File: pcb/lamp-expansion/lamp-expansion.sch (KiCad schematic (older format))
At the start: 18 parts

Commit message: schematic work for expansion board
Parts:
- added BT?: LIPO, symbol LIPO
- added C? (x2): 22uF, symbol C_POL
- added C? (x2): 10uF, symbol C_POL
- added D?: PMEG2020CPA, symbol SCHOTTKY_DUAL-CC
- added D?: MSS2P2, symbol D_SCHOTTKY
- added IC?: LM1117_5.0, symbol LM1117
- added J?: 6-15V, symbol DCIN
- C?: value 4.7uF -> 10uF; Distrib. Part (none) -> 587-1353-1-ND; Distributor (none) -> Digikey; Manuf. Part (none) -> Taiyo Yuden; Manufacturer (none) -> TMK316F106ZL-T
- IC?: value LM1117 -> LM1117_3.3; Distrib. Part (none) -> AP1117IE33G-13DICT-ND; Distributor (none) -> Digikey; Manuf. Part (none) -> AP1117IE33G-13; Manufacturer (none) -> Diodes Incorporated
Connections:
- net labels added: +5V, +BATT, DC_IN, VCC, V_DC
- wire segments 45 -> 71
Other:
- note added: "DC input and 3.3V LDO"
- note added: "lithium polymer battery and charger"
- moved on the sheet: IC?

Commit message: work in progress
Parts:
- removed D?: PMEG2020CPA, symbol SCHOTTKY_DUAL-CC
- added C? (x4): 1uF, symbol C
- added C? (x2): 0.1uF, symbol C
- added D? (x2): MSS2P2, symbol D_SCHOTTKY
- added IC?: MCP73811, symbol MCP73811/2
- added IC?: AP2411, symbol AP24x1
- added IC?: TLV1117LV28, symbol LM1117
- added JP?: WIFI-LOG-LVL, symbol JUMPER
- added JP?: BAT-TO-REG, symbol JUMPER
- added JP?: BAT-TO-VCC, symbol JUMPER-CLOSED
- added J_SPI: 2x3PIN_FEMALE, symbol 6PIN_FEMALE
- added J_UART: 6PIN_FEMALE, symbol 6PIN_FEMALE
- added R?: 10kΩ, symbol R
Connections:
- net labels added: AVR_MISO, AVR_MOSI, AVR_RST, AVR_SCK, V_BAT, V_IO
- net labels removed: DC_IN
- wire segments 71 -> 156
- no-connect marks 2 -> 3
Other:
- note added: "2.8V regulator for wifi logic level"
- note added: "3.3V jumper for wifi logic level"
- note added: "5V charger input"
- note added: "battery and charger"
- note added: "battery voltage switching jumpers"
- note added: "lithium polymer battery, charger, and power switch"
- note added: "power switch"
- note removed: "lithium polymer battery and charger"
- moved on the sheet: BT?, C?, D?, F?, IC?, J?, R?, RX, TX

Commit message: cc3000 schematic diagram done
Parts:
- removed JP?: WIFI-LOG-LVL, symbol JUMPER
- removed JP?: BAT-TO-REG, symbol JUMPER
- removed JP?: BAT-TO-VCC, symbol JUMPER-CLOSED
- added AE?: ANTENNA, symbol ANTENNA
- added C? (x2): 1uF, symbol C
- added C?: 10pF, symbol C
- added C?: 2.2pF, symbol C
- added C?: DNP(10pF), symbol C
- added J?: UF.L, symbol COAX-JACK
- added JP?: VBAT-DIR-SELECT, symbol JUMPER_3-PIN-CLOSED
- added JP?: WIFI-LOG-LVL-SEL, symbol JUMPER_2-PIN
- added JP?: MODE-SEL, symbol JUMPER_3-PIN-CLOSED
- added L?: 2.2nH, symbol L
- added L?: DNP, symbol L
- added R?: 0Ω, symbol R
- added TP1, TP2, TP3, TP4, TP5: TEST, symbol TEST
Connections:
- net labels added: CC_EN, CC_IRQ, CC_MISO, CC_MOSI, CC_SCK, CC_SEL
- wire segments 156 -> 187
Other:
- note added: "CC3000 wifi module"
- note added: "optional external antenna jack"
- note added: "wifi logic 3.3V jumper"
- note removed: "3.3V jumper for wifi logic level"
- moved on the sheet: BT?, C?, D?, F?, IC?, J?, J_SPI, J_UART, R?, RX, TX

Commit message: moving to work on main board
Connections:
- net GND: now also C?.1
- net VCC: now also C?.2, IC?.19 (VBAT_IN)
- net V_FTDI: now also IC?.10 (3V3OUT)
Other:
- moved on the sheet: D?, J?
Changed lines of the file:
@@
 L DCIN J?
 U 1 1 5355B2AC
-P 1500 6350
-F 0 "J?" H 1450 6100 60  0000 C CNN
-F 1 "6-15V" H 1500 6000 60  0000 C CNN
-F 2 "" H 1500 6350 60  0000 C CNN
-F 3 "" H 1500 6350 60  0000 C CNN
-	1    1500 6350
+P 1600 6350
+F 0 "J?" H 1550 6100 60  0000 C CNN
+F 1 "6-15V" H 1600 6000 60  0000 C CNN
+F 2 "" H 1600 6350 60  0000 C CNN
+F 3 "" H 1600 6350 60  0000 C CNN
+	1    1600 6350
 	1    0    0    -1
 $EndComp
@@
 L GND #PWR?
 U 1 1 5355B2CA
-P 1850 6500
-F 0 "#PWR?" H 1850 6500 30  0001 C CNN
-F 1 "GND" H 1850 6430 30  0001 C CNN
-F 2 "" H 1850 6500 60  0000 C CNN
-F 3 "" H 1850 6500 60  0000 C CNN
-	1    1850 6500
+P 1950 6500
+F 0 "#PWR?" H 1950 6500 30  0001 C CNN
+F 1 "GND" H 1950 6430 30  0001 C CNN
+F 2 "" H 1950 6500 60  0000 C CNN
+F 3 "" H 1950 6500 60  0000 C CNN
+	1    1950 6500
 	1    0    0    -1
 $EndComp
@@
 	0    1    1    0
 $EndComp
-Text Label 2550 6300 2    60   ~ 0
+Text Label 2650 6300 2    60   ~ 0
 V_DC
 $Comp
@@
 	3700 8400 3700 8200
 Wire Wire Line
-	3700 8200 4200 8200
+	3700 8200 4300 8200
 Wire Wire Line
 	5400 8700 5300 8700
@@
 	5850 8300 5300 8300
 Wire Wire Line
-	1850 6500 1850 6400
-Wire Wire Line
-	1850 6400 1750 6400
+	1950 6500 1950 6400
+Wire Wire Line
+	1950 6400 1850 6400
 Wire Wire Line
 	3350 6200 3750 6200
@@
 L D_SCHOTTKY D?
 U 1 1 5356B181
-P 2000 6300
-F 0 "D?" H 2000 6500 60  0000 C CNN
-F 1 "MSS2P2" H 2000 6400 60  0000 C CNN
-F 2 "" H 1750 6300 60  0001 C CNN
-F 3 "" H 1850 6400 60  0001 C CNN
-F 4 "Vishay" H 2000 6300 60  0001 C CNN "Manufacturer"
-F 5 "MSS2P2-M3/89A" H 2000 6300 60  0001 C CNN "Manuf. Part"
-F 6 "Digikey" H 2000 6300 60  0001 C CNN "Distributor"
-F 7 "MSS2P2-M3/89AGICT-ND" H 2000 6300 60  0001 C CNN "Distrib. Part"
-	1    2000 6300
-	1    0    0    -1
-$EndComp
-Wire Wire Line
-	1750 6300 1850 6300
-Wire Wire Line
-	2550 6300 2150 6300
+P 2100 6300
+F 0 "D?" H 2100 6500 60  0000 C CNN
+F 1 "MSS2P2" H 2100 6400 60  0000 C CNN
+F 2 "" H 1850 6300 60  0001 C CNN
+F 3 "" H 1950 6400 60  0001 C CNN
+F 4 "Vishay" H 2100 6300 60  0001 C CNN "Manufacturer"
+F 5 "MSS2P2-M3/89A" H 2100 6300 60  0001 C CNN "Manuf. Part"
+F 6 "Digikey" H 2100 6300 60  0001 C CNN "Distributor"
+F 7 "MSS2P2-M3/89AGICT-ND" H 2100 6300 60  0001 C CNN "Distrib. Part"
+	1    2100 6300
+	1    0    0    -1
+$EndComp
+Wire Wire Line
+	1850 6300 1950 6300
+Wire Wire Line
+	2650 6300 2250 6300
 Wire Wire Line
 	3200 6600 3500 6600
@@
 	0    -1   -1   0
 $EndComp
-Wire Wire Line
-	14250 5150 14050 5150
 $Comp
 L GND #PWR?
@@
 U 1 1 53570C4B
 P 14150 4650
-F 0 "C?" V 14150 4950 60  0000 C CNN
+F 0 "C?" V 14150 5000 60  0000 C CNN
 F 1 "1uF" V 14250 5000 60  0000 C CNN
 F 2 "" H 14150 4650 60  0001 C CNN
@@
 F 3 "" H 14250 5350 60  0000 C CNN
 	1    14250 5350
-	0    1    1    0
-$EndComp
-$Comp
-L C C?
-U 1 1 5357209E
-P 14150 5250
-F 0 "C?" V 14100 5600 60  0000 C CNN
-F 1 "1uF" V 14200 5600 60  0000 C CNN
-F 2 "" H 14150 5250 60  0001 C CNN
-F 3 "" H 14150 5250 60  0001 C CNN
-	1    14150 5250
 	0    1    1    0
 $EndComp
@@
 Wire Notes Line
 	14650 6600 13500 6600
+Wire Wire Line
+	14050 5350 14250 5350
+Connection ~ 14150 5350
+$Comp
+L C C?
+U 1 1 5357209E
+P 14150 5250
+F 0 "C?" V 14100 5600 60  0000 C CNN
+F 1 "1uF" V 14200 5600 60  0000 C CNN
+F 2 "" H 14150 5250 60  0001 C CNN
+F 3 "" H 14150 5250 60  0001 C CNN
+	1    14150 5250
+	0    1    1    0
+$EndComp
+Wire Wire Line
+	14050 5150 14250 5150
+Connection ~ 14150 5150
 $EndSCHEMATC

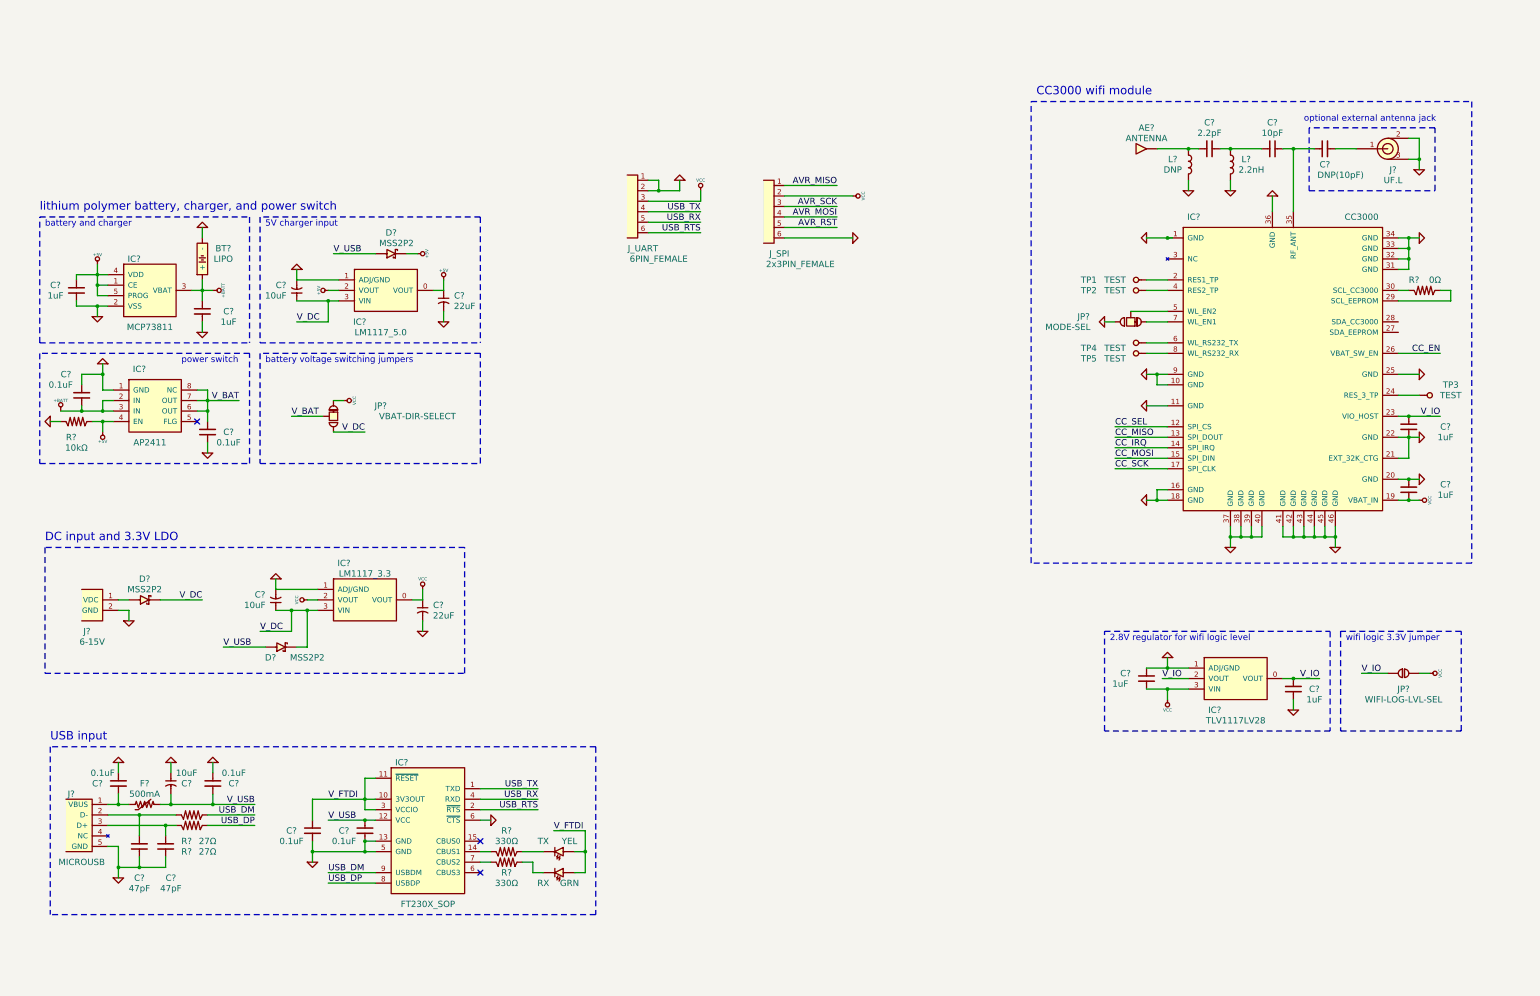
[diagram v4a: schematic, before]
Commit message: still need to add boost reg to schematic;
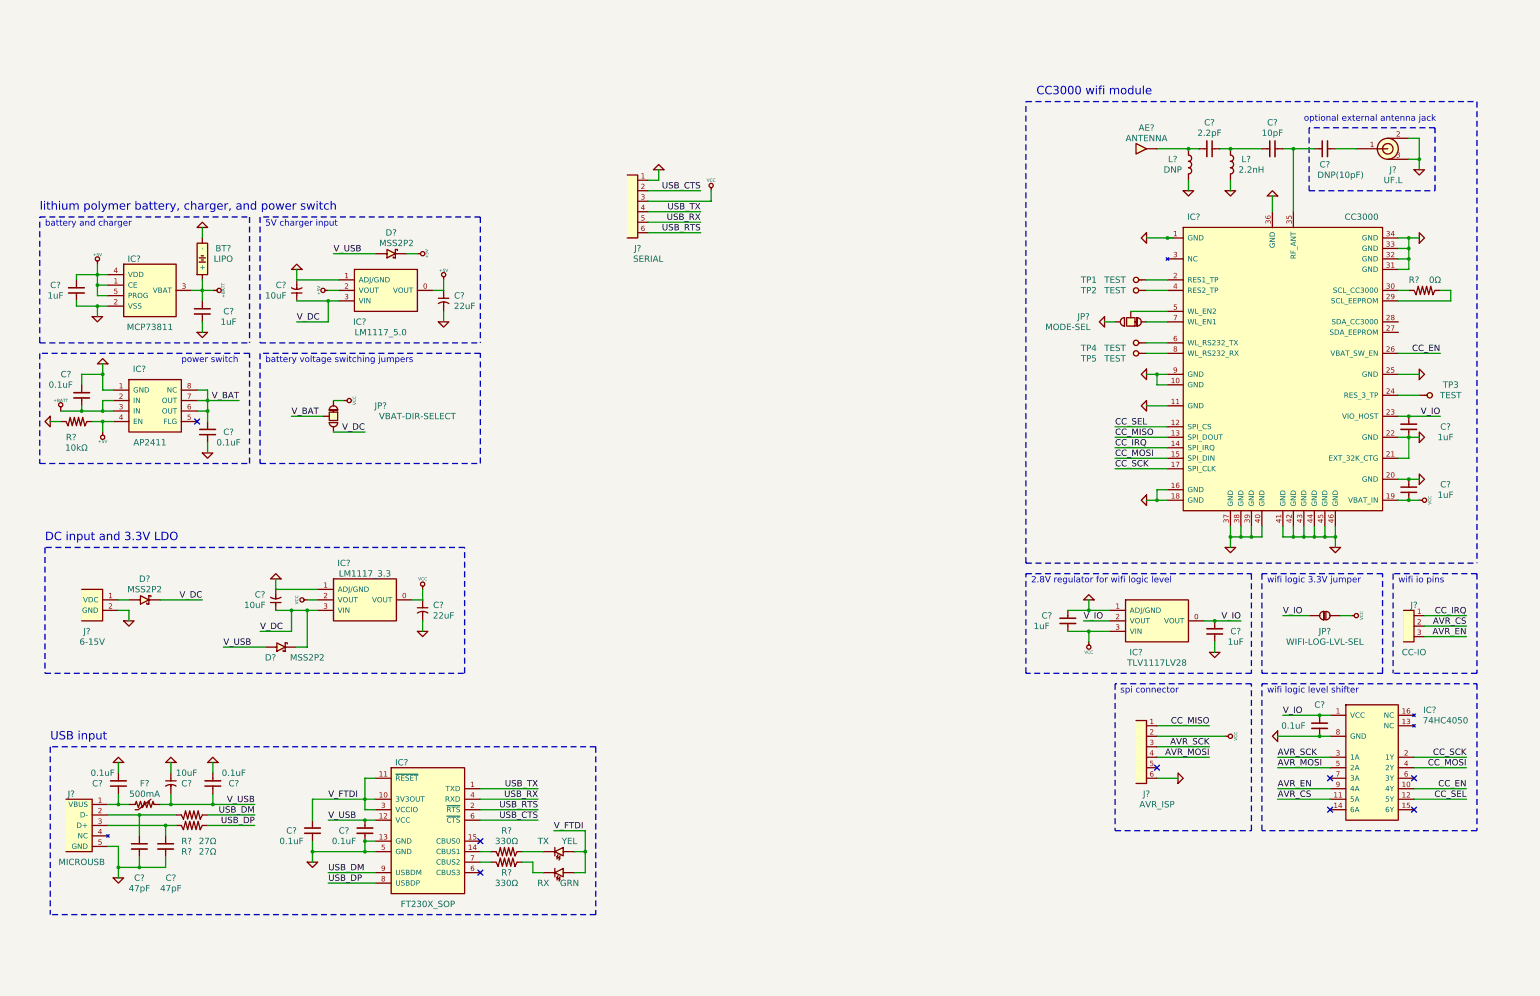
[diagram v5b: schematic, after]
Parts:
- added C?: 0.1uF, symbol C
- added IC?: 74HC4050, symbol 74HC4050
- added J?: CC-IO, symbol 3PIN_FEMALE
- J?: renamed from J_UART; value 6PIN_FEMALE -> SERIAL
- J?: renamed from J_SPI; value 2x3PIN_FEMALE -> AVR_ISP
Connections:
- net AVR_MISO is gone; now on net CC_MISO: J?.1
- net AVR_MOSI: now also IC?.5 (2A)
- net AVR_SCK: now also IC?.3 (1A)
- net CC_EN: now also IC?.10 (4Y)
- net CC_IRQ: now also J?.1
- net CC_MOSI: now also IC?.4 (2Y)
- net CC_SCK: now also IC?.2 (1Y)
- net CC_SEL: now also IC?.12 (5Y)
- net GND: now also C?.2, IC?.8 (GND); no longer IC?.6 (~CTS~), J?.2
- net V_IO: now also C?.1, IC?.1 (VCC)
- net USB_CTS: now reaches IC?.6 (~CTS~)
- net USB_CTS: now also J?.2
- net AVR_RST: no longer names the net of J?.5
- new net AVR_CS: IC?.11 (5A), J?.2
- new net AVR_EN: IC?.9 (4A), J?.3
- no-connect marks 3 -> 8
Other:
- note added: "spi connector"
- note added: "wifi io pins"
- note added: "wifi logic level shifter"
- moved on the sheet: C?, IC?, J?, JP?

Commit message: expansion schematic nearly done
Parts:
- removed C? (x2): 22uF, symbol C_POL
- added C?: 4.7pF, symbol C_POL
- added C? (x3): 22uF, symbol C_POL
- added C? (x2): 0.1uF, symbol C
- added C?: 100uF, symbol C_POL
- added D? (x2): 3A, symbol D_SCHOTTKY
- added IC?: LM2623_VSSOP, symbol LM2623_VSSOP
- added IC?: 78L50_SOT, symbol 78LXX_SOT
- added JP?: I-TEST, symbol JUMPER_2-PIN-CLOSED
- added L?: 4.7uH, symbol L
- added Q?: 2N7002, symbol N-CHAN-MOSFET_SOT
- added R?: 10k, symbol R
- added R?: 150kΩ, symbol R
- added R?: 430kΩ, symbol R
- added R?: 91kΩ, symbol R
- J?: value 6-15V -> 7-15V
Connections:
- net +5V: now also C?.1
- net GND: now also C?.1, C?.2, C?.2, C?.2, C?.2, C?.2, IC?.1 (PGND), IC?.5 (SGND), Q?.2 (S), R?.2
- net VCC: now also C?.1
- net V_BAT: now also C?.1, D?.1 (C), D?.2 (A), L?.1, R?.2
- net V_USB: now also D?.2 (A)
- net DC_IN: now reaches D?.2 (A), J?.1 (VDC)
- net DC_IN: now also Q?.1 (G)
- new net: IC?.2 (EN), Q?.3 (D), R?.1
- new net: C?.1, IC?.3 (FREQ), R?.1
- new net: IC?.4 (FB), R?.1, R?.2
- new net: C?.2, IC?.6 (VDD), R?.2
- new net: C?.2, IC?.8 (SW), JP?.1
- new net: JP?.1, L?.2
- new net V_LED: C?.1, C?.1, D?.1 (C), IC?.7 (BOOT), R?.1
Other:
- note added: "USB / battery to 7V boost regulator"
- moved on the sheet: AE?, BT?, C?, D?, F?, IC?, J?, JP?, L?, R?, RX, TP1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

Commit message: i think the schematic is done
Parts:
- added J? (x2): 2PIN_POWER, symbol 2PIN_FEMALE
- added J?: 2PIN_IO, symbol 2PIN_FEMALE
- added J?: 5PIN_INPUT, symbol 5PIN_FEMALE
- added R? (x2): 10kΩ, symbol R
- added S? (x2): SPST, symbol SPST
- added TP? (x7): PIN, symbol TEST
- added VR? (x3): 100kΩ, symbol POT
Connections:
- net GND: now also J?.2, J?.2, S?.1, S?.1, VR?.3 (E2), VR?.3 (E2), VR?.3 (E2)
- net VCC: now also J?.1, R?.1, R?.1, VR?.1 (E1), VR?.1 (E1), VR?.1 (E1)
- net V_LED: now also J?.1
- new net AVR_0: J?.1, TP?.1 (TP)
- new net AVR_1: J?.2, TP?.1 (TP)
- new net POT_0: J?.1, TP?.1 (TP), VR?.2 (W)
- new net POT_1: J?.2, TP?.1 (TP), VR?.2 (W)
- new net POT_2: J?.3, TP?.1 (TP), VR?.2 (W)
- new net SW_0: J?.4, R?.2, S?.2, TP?.1 (TP)
- new net SW_1: J?.5, R?.2, S?.2, TP?.1 (TP)
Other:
- note added: "buttons"
- note added: "buttons and pots header"
- note added: "extra io"
- note added: "potentiometers"
- note added: "power headers"
- note added: "serial header"
- note added: "user input"
- moved on the sheet: J?

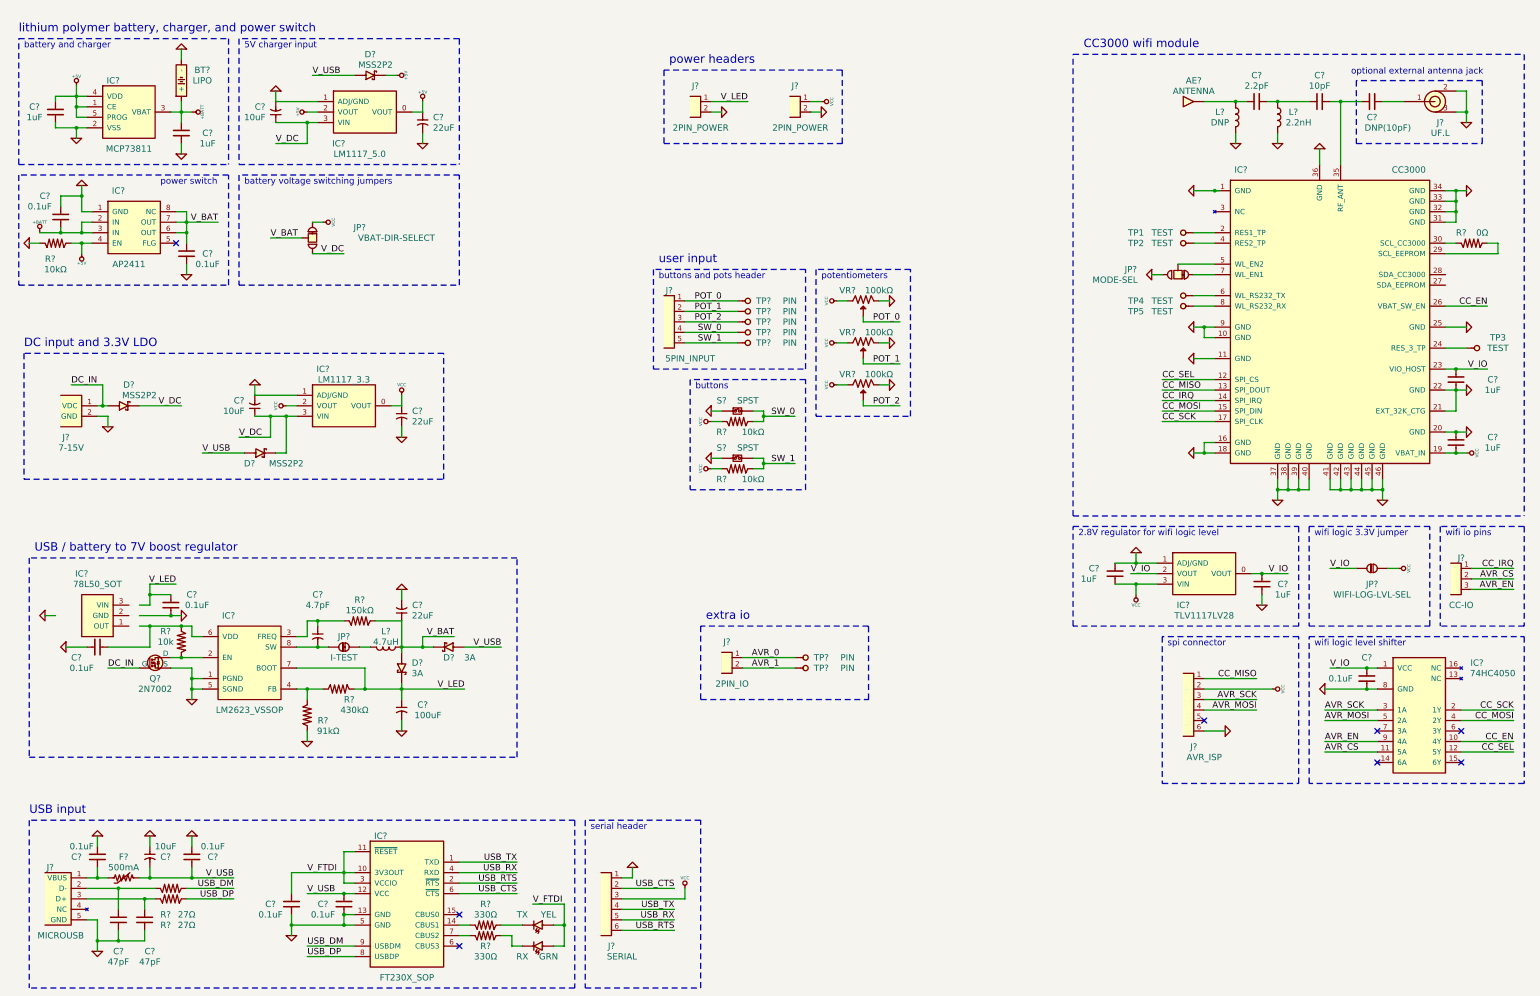
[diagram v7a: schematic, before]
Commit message: schematic passes error checking
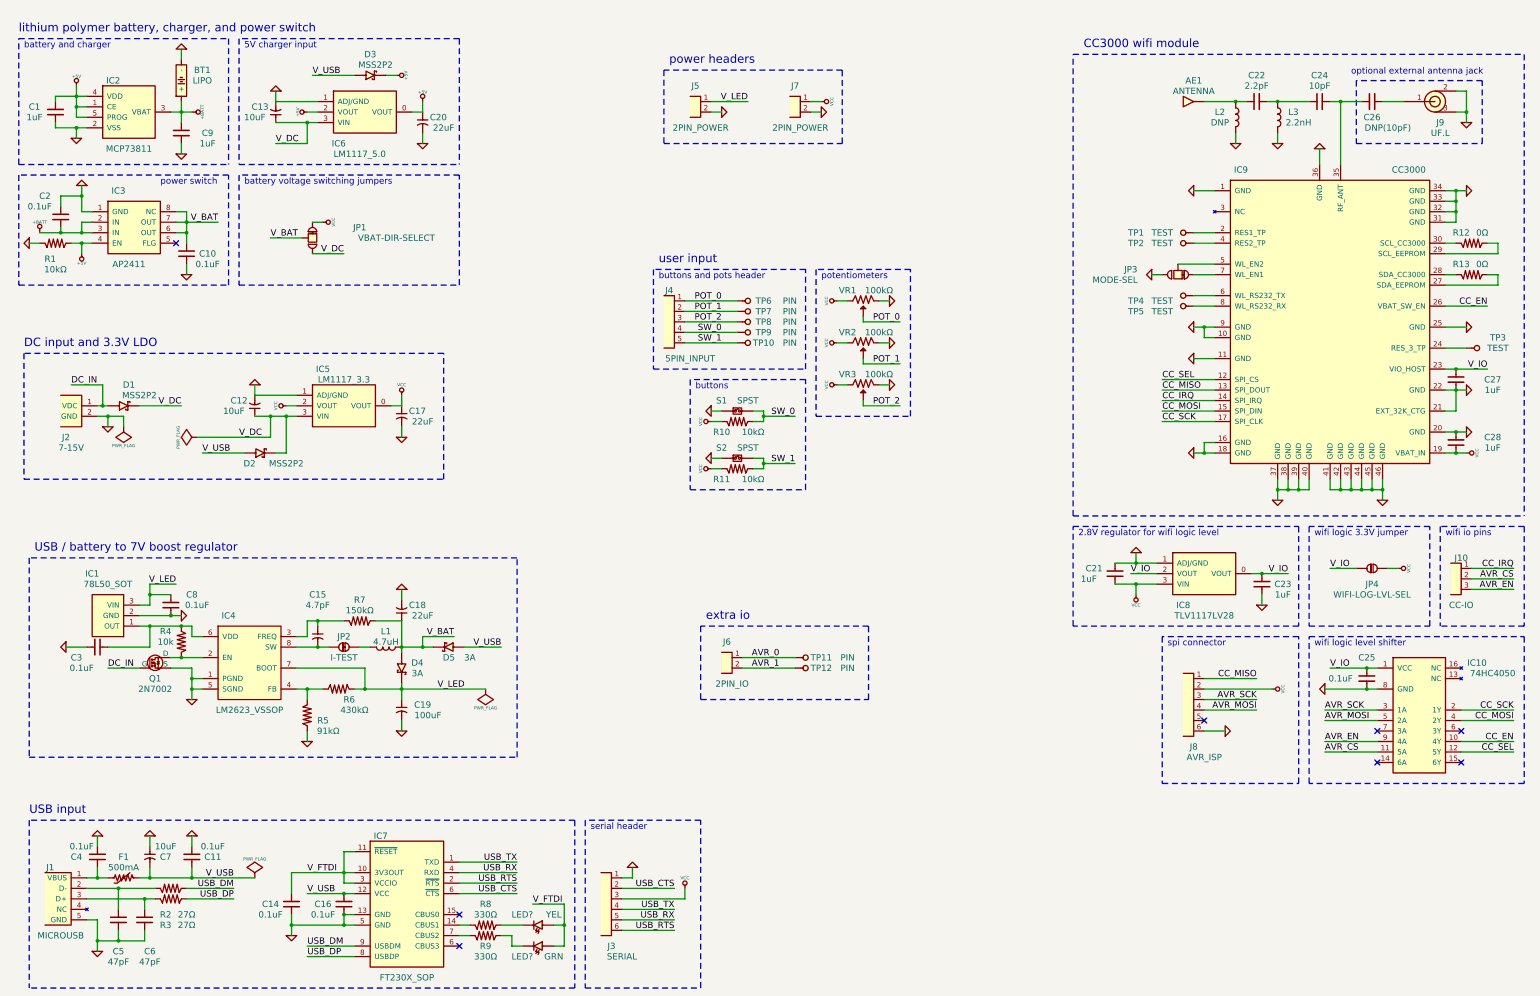
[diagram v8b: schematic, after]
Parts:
- added R13: 0Ω, symbol R
- gave numbers to parts that had none: 88
- renumbered RX to LED?, TX to LED?
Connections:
- net GND: now also IC1.2 (GND)
- net V_LED: now also IC1.3 (VIN)
- net at IC9.27 (SDA_EEPROM): now also R13.2
- net at IC9.28 (SDA_CC3000): now also R13.1
- net at C3.2, IC4.6 (VDD), R4.2: now also IC1.1 (OUT)
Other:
- moved on the sheet: IC1
